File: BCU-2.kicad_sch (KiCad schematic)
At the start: 10 parts, among them J2 Conn_01x12_Male, J6 Conn_01x04_Male, J7 Conn_01x04_Male, U1 Teensy3.2

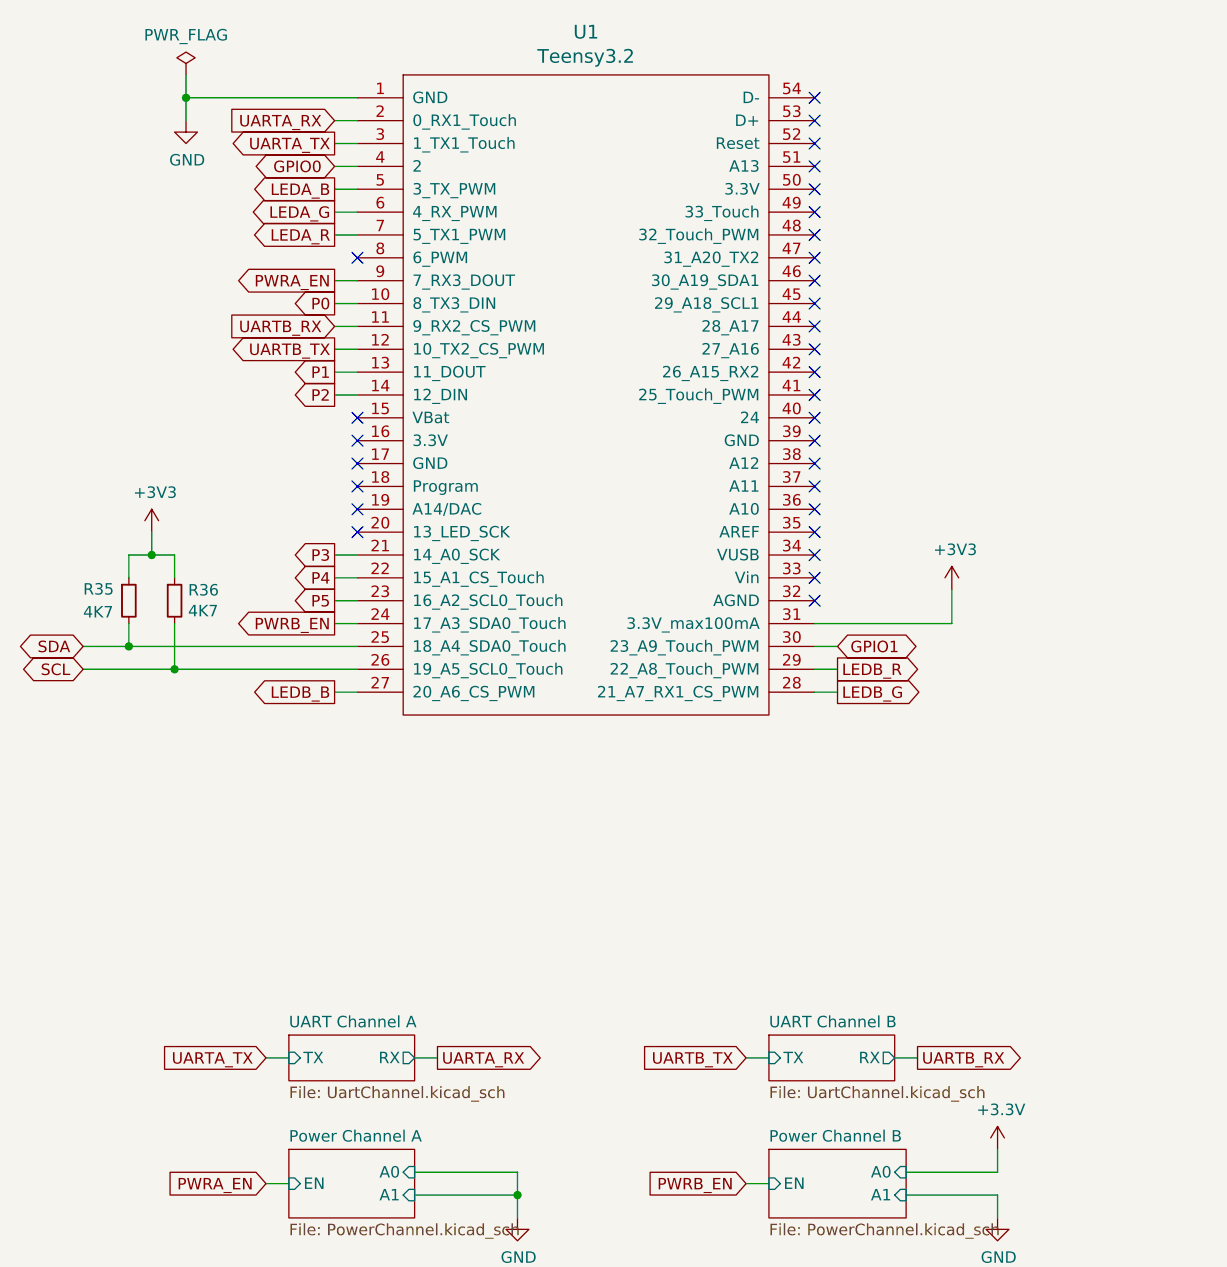
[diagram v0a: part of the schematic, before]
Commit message: Schematic: Remove UART channels
Signed-off-by: Geert Uytterhoeven <geert@linux-m68k.org>
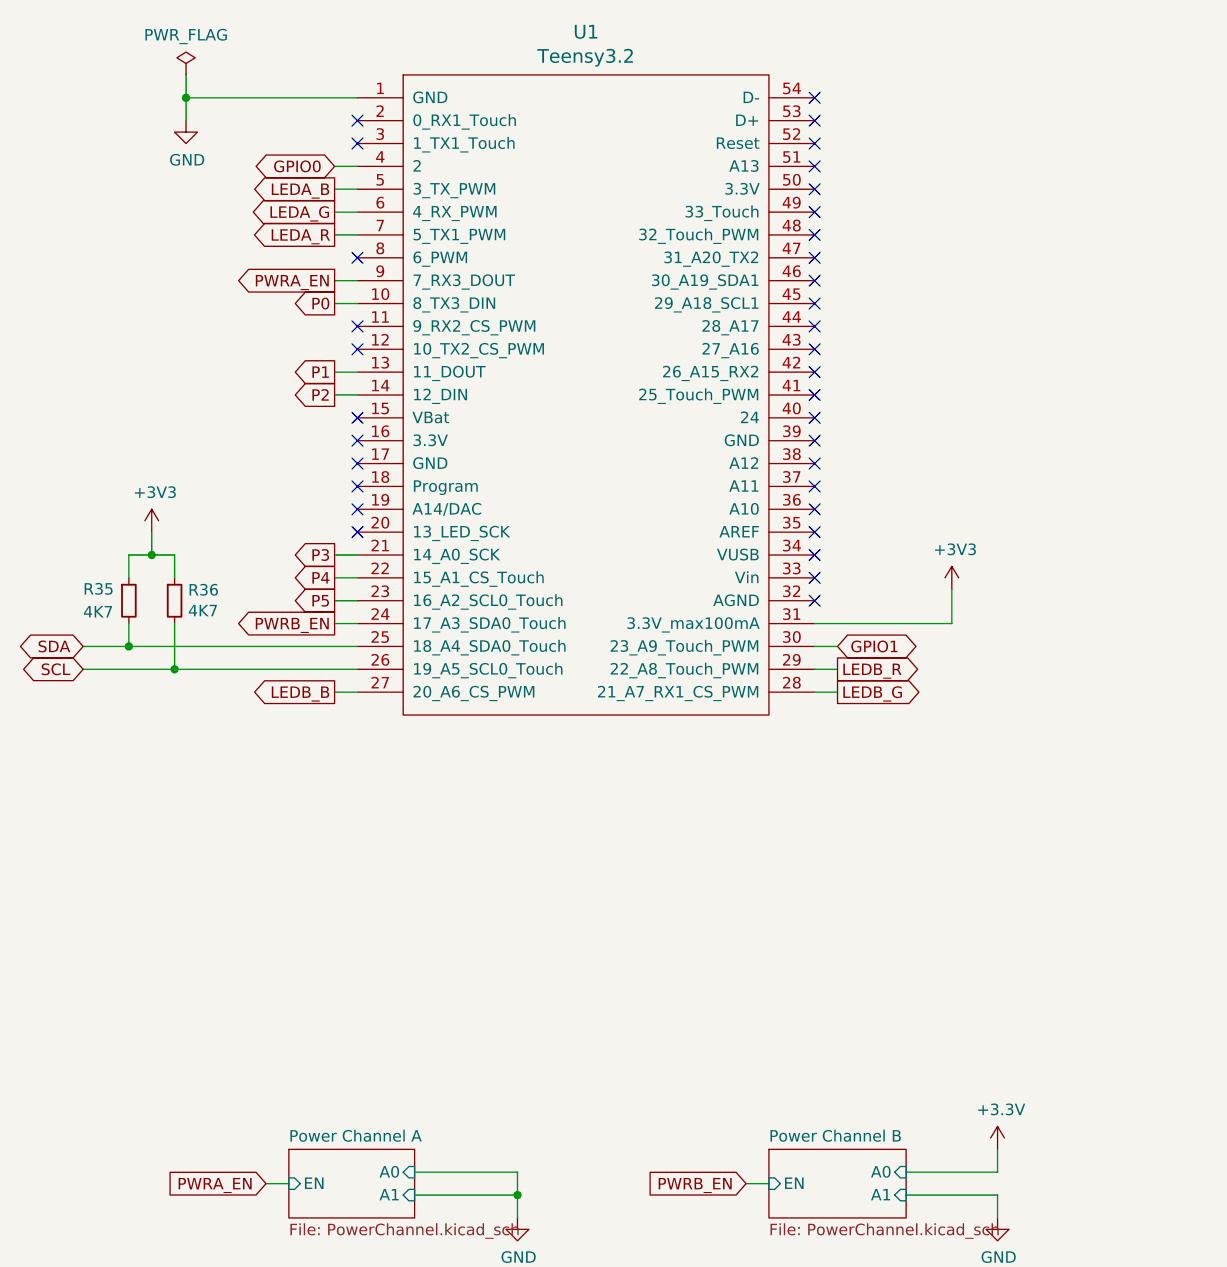
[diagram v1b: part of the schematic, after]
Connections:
- net UARTA_RX: no longer names the net of U1.2 (0_RX1_Touch)
- net UARTA_TX: no longer names the net of U1.3 (1_TX1_Touch)
- net UARTB_RX: no longer names the net of U1.11 (9_RX2_CS_PWM)
- net UARTB_TX: no longer names the net of U1.12 (10_TX2_CS_PWM)
- no-connect marks 30 -> 34
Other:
- removed sheet UART Channel A
- removed sheet UART Channel B

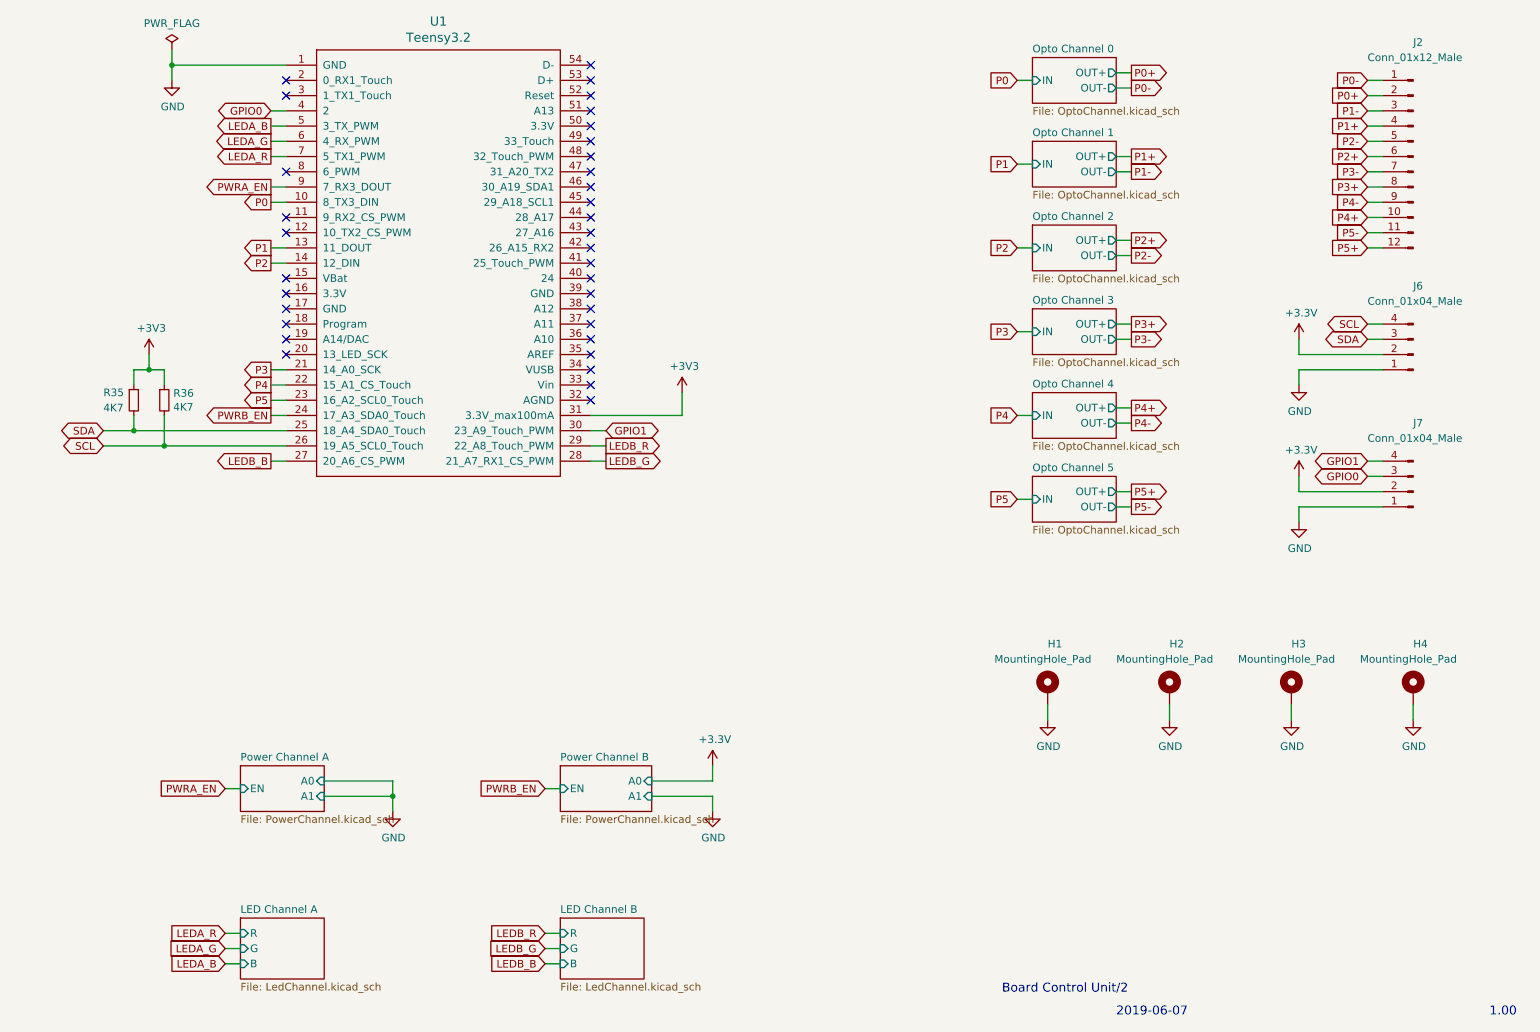
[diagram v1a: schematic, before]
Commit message: Schematic: Remove LED channels
Signed-off-by: Geert Uytterhoeven <geert@linux-m68k.org>
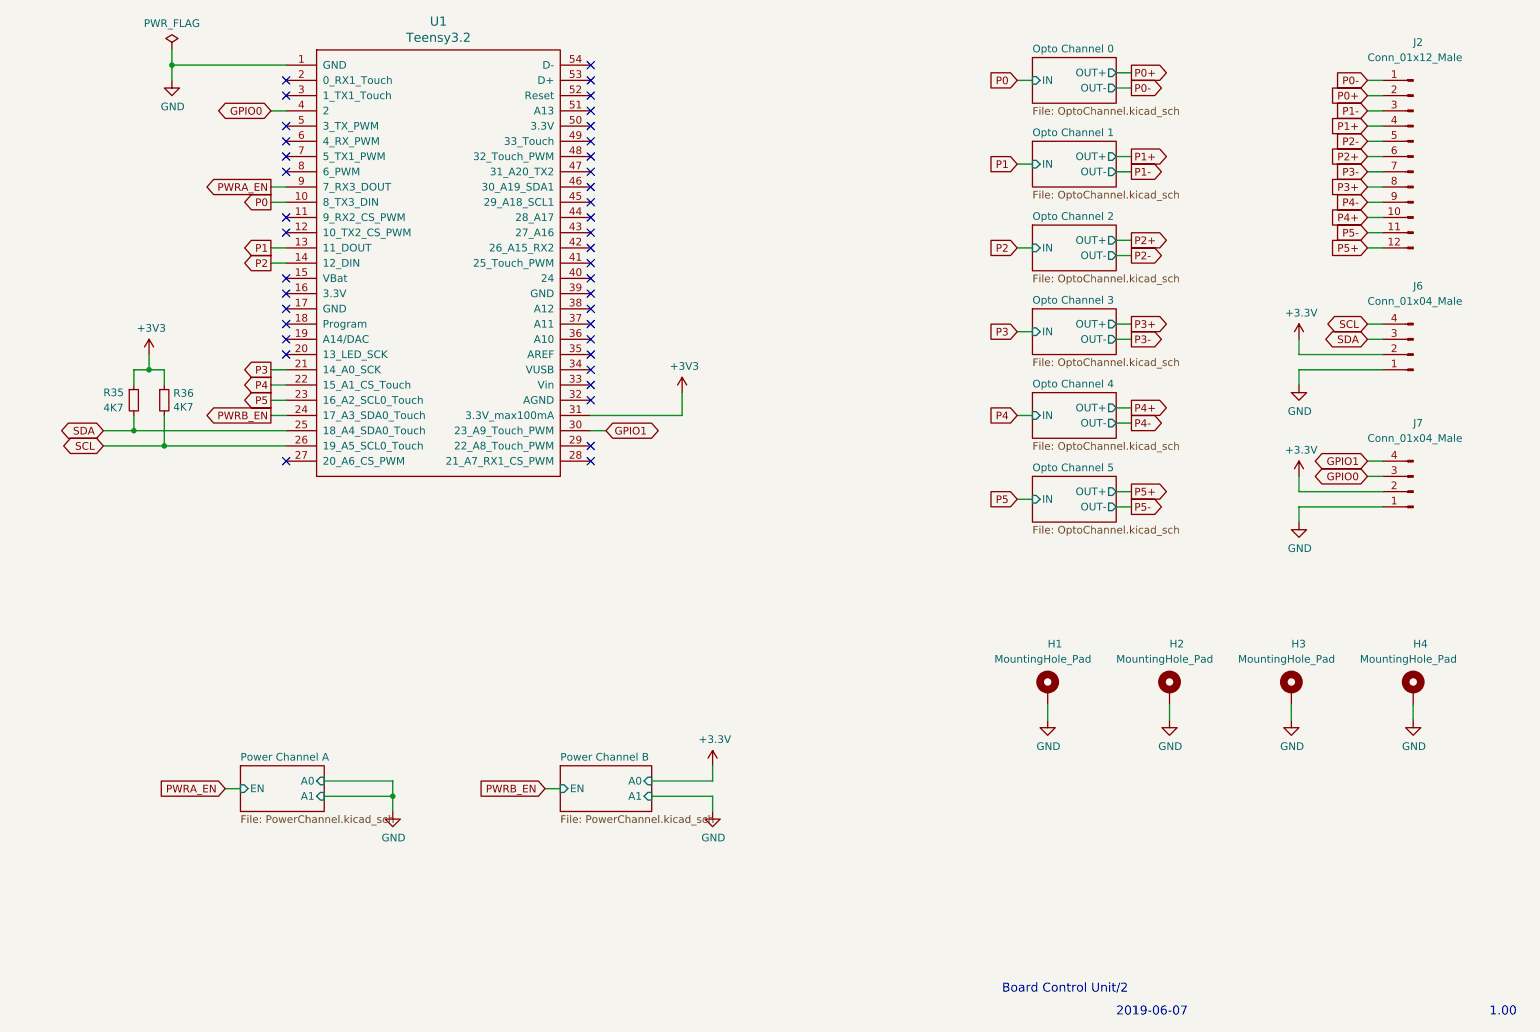
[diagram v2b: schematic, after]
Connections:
- net LEDA_B: no longer names the net of U1.5 (3_TX_PWM)
- net LEDA_G: no longer names the net of U1.6 (4_RX_PWM)
- net LEDA_R: no longer names the net of U1.7 (5_TX1_PWM)
- net LEDB_B: no longer names the net of U1.27 (20_A6_CS_PWM)
- net LEDB_G: no longer names the net of U1.28 (21_A7_RX1_CS_PWM)
- net LEDB_R: no longer names the net of U1.29 (22_A8_Touch_PWM)
- no-connect marks 34 -> 40
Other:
- removed sheet LED Channel A
- removed sheet LED Channel B

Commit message: Schematic: Remove GPIO expansion connector
Signed-off-by: Geert Uytterhoeven <geert@linux-m68k.org>
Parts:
- removed J7: Conn_01x04_Male, Connector_JST:JST_PH_B4B-PH-K_1x04_P2.00mm_Vertical, symbol Connector:Conn_01x04_Male
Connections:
- net GPIO0: no longer names the net of U1.4 (2)
- net GPIO1: no longer names the net of U1.30 (23_A9_Touch_PWM)
- no-connect marks 40 -> 42
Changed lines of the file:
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@@
   (no_connect (at 68.58 71.12))
   (no_connect (at 119.38 40.64))
+  (no_connect (at 119.38 96.52))
   (no_connect (at 68.58 45.72))
   (no_connect (at 119.38 38.1))
   (no_connect (at 68.58 81.28))
   (no_connect (at 68.58 60.96))
+  (no_connect (at 68.58 43.18))
   (no_connect (at 68.58 53.34))
   (no_connect (at 68.58 76.2))
@@
     (stroke (width 0) (type default) (color 0 0 0 0))
   )
-  (wire (pts (xy 248.92 101.6) (xy 251.46 101.6))
-    (stroke (width 0) (type default) (color 0 0 0 0))
-  )
   (wire (pts (xy 251.46 40.64) (xy 248.92 40.64))
     (stroke (width 0) (type default) (color 0 0 0 0))
   )
-  (wire (pts (xy 251.46 104.14) (xy 248.92 104.14))
-    (stroke (width 0) (type default) (color 0 0 0 0))
-  )
-  (wire (pts (xy 237.49 106.68) (xy 237.49 104.14))
-    (stroke (width 0) (type default) (color 0 0 0 0))
-  )
-  (wire (pts (xy 119.38 96.52) (xy 121.92 96.52))
-    (stroke (width 0) (type default) (color 0 0 0 0))
-  )
   (wire (pts (xy 207.01 92.71) (xy 209.55 92.71))
     (stroke (width 0) (type default) (color 0 0 0 0))
@@
     (stroke (width 0) (type default) (color 0 0 0 0))
   )
-  (wire (pts (xy 251.46 109.22) (xy 237.49 109.22))
-    (stroke (width 0) (type default) (color 0 0 0 0))
-  )
   (wire (pts (xy 251.46 83.82) (xy 237.49 83.82))
     (stroke (width 0) (type default) (color 0 0 0 0))
@@
     (stroke (width 0) (type default) (color 0 0 0 0))
   )
-  (wire (pts (xy 66.04 43.18) (xy 68.58 43.18))
-    (stroke (width 0) (type default) (color 0 0 0 0))
-  )
   (wire (pts (xy 129.54 154.94) (xy 139.7 154.94))
     (stroke (width 0) (type default) (color 0 0 0 0))
@@
     (stroke (width 0) (type default) (color 0 0 0 0))
   )
-  (wire (pts (xy 251.46 106.68) (xy 237.49 106.68))
-    (stroke (width 0) (type default) (color 0 0 0 0))
-  )
   (wire (pts (xy 248.92 78.74) (xy 251.46 78.74))
-    (stroke (width 0) (type default) (color 0 0 0 0))
-  )
-  (wire (pts (xy 237.49 109.22) (xy 237.49 111.76))
     (stroke (width 0) (type default) (color 0 0 0 0))
   )
@@
     )
   )
-  (global_label "GPIO0" (shape bidirectional) (at 66.04 43.18 180) (fields_autoplaced)
-    (effects (font (size 1.27 1.27)) (justify right))
-    (property "Intersheet References" "${INTERSHEET_REFS}" (id 0) (at 0 0 0)
-      (effects (font (size 1.27 1.27)) hide)
-    )
-  )
   (global_label "PWRA_EN" (shape input) (at 58.42 156.21 180) (fields_autoplaced)
     (effects (font (size 1.27 1.27)) (justify right))
@@
   (global_label "P1" (shape input) (at 190.5 52.07 180) (fields_autoplaced)
     (effects (font (size 1.27 1.27)) (justify right))
-    (property "Intersheet References" "${INTERSHEET_REFS}" (id 0) (at 0 0 0)
-      (effects (font (size 1.27 1.27)) hide)
-    )
-  )
-  (global_label "GPIO1" (shape bidirectional) (at 121.92 96.52 0) (fields_autoplaced)
-    (effects (font (size 1.27 1.27)) (justify left))
     (property "Intersheet References" "${INTERSHEET_REFS}" (id 0) (at 0 0 0)
       (effects (font (size 1.27 1.27)) hide)
@@
     )
   )
-  (global_label "GPIO1" (shape bidirectional) (at 248.92 101.6 180) (fields_autoplaced)
-    (effects (font (size 1.27 1.27)) (justify right))
-    (property "Intersheet References" "${INTERSHEET_REFS}" (id 0) (at 0 0 0)
-      (effects (font (size 1.27 1.27)) hide)
-    )
-  )
   (global_label "P4+" (shape output) (at 209.55 92.71 0) (fields_autoplaced)
     (effects (font (size 1.27 1.27)) (justify left))
@@
   )
   (global_label "PWRB_EN" (shape input) (at 111.76 156.21 180) (fields_autoplaced)
-    (effects (font (size 1.27 1.27)) (justify right))
-    (property "Intersheet References" "${INTERSHEET_REFS}" (id 0) (at 0 0 0)
-      (effects (font (size 1.27 1.27)) hide)
-    )
-  )
-  (global_label "GPIO0" (shape bidirectional) (at 248.92 104.14 180) (fields_autoplaced)
     (effects (font (size 1.27 1.27)) (justify right))
     (property "Intersheet References" "${INTERSHEET_REFS}" (id 0) (at 0 0 0)
@@
     (pin "1")
   )
-  (symbol (lib_id "Connector:Conn_01x04_Male") (at 256.54 106.68 180) (unit 1)
-    (in_bom yes) (on_board yes)
-    (property "Reference" "J7" (id 0) (at 256.54 95.25 0)
-      (effects (font (size 1.27 1.27)) (justify right))
-    )
-    (property "Value" "Conn_01x04_Male" (id 1) (at 248.92 97.79 0)
-      (effects (font (size 1.27 1.27)) (justify right))
-    )
-    (property "Footprint" "Connector_JST:JST_PH_B4B-PH-K_1x04_P2.00mm_Vertical" (id 2) (at 256.54 106.68 0)
-      (effects (font (size 1.27 1.27)) hide)
-    )
-    (property "Datasheet" "~" (id 3) (at 256.54 106.68 0)
-      (effects (font (size 1.27 1.27)) hide)
-    )
-    (pin "1")
-    (pin "2")
-    (pin "3")
-    (pin "4")
-  )
-  (symbol (lib_id "power:GND") (at 237.49 111.76 0) (unit 1)
-    (in_bom yes) (on_board yes)
-    (property "Reference" "#PWR0115" (id 0) (at 237.49 118.11 0)
-      (effects (font (size 1.27 1.27)) hide)
-    )
-    (property "Value" "GND" (id 1) (at 237.617 116.1542 0))
-    (property "Footprint" "" (id 2) (at 237.49 111.76 0)
-      (effects (font (size 1.27 1.27)) hide)
-    )
-    (property "Datasheet" "" (id 3) (at 237.49 111.76 0)
-      (effects (font (size 1.27 1.27)) hide)
-    )
-    (pin "1")
-  )
-  (symbol (lib_id "power:+3.3V") (at 237.49 104.14 0) (unit 1)
-    (in_bom yes) (on_board yes)
-    (property "Reference" "#PWR0116" (id 0) (at 237.49 107.95 0)
-      (effects (font (size 1.27 1.27)) hide)
-    )
-    (property "Value" "+3.3V" (id 1) (at 237.871 99.7458 0))
-    (property "Footprint" "" (id 2) (at 237.49 104.14 0)
-      (effects (font (size 1.27 1.27)) hide)
-    )
-    (property "Datasheet" "" (id 3) (at 237.49 104.14 0)
-      (effects (font (size 1.27 1.27)) hide)
-    )
-    (pin "1")
-  )
   (symbol (lib_id "Connector:Conn_01x12_Male") (at 256.54 50.8 0) (mirror y) (unit 1)
     (in_bom yes) (on_board yes)
@@
       (reference "#PWR0112") (unit 1) (value "+3V3") (footprint "")
     )
-    (path "/00000000-0000-0000-0000-00005ce94ab6"
-      (reference "#PWR0115") (unit 1) (value "GND") (footprint "")
-    )
-    (path "/00000000-0000-0000-0000-00005ce94abc"
-      (reference "#PWR0116") (unit 1) (value "+3.3V") (footprint "")
-    )
     (path "/00000000-0000-0000-0000-00005be8d10d/00000000-0000-0000-0000-00005ce3761d"
       (reference "C5") (unit 1) (value "100n") (footprint "Capacitor_SMD:C_0603_1608Metric_Pad1.05x0.95mm_HandSolder")
@@
       (reference "J6") (unit 1) (value "Conn_01x04_Male") (footprint "Connector_JST:JST_PH_B4B-PH-K_1x04_P2.00mm_Vertical")
     )
-    (path "/00000000-0000-0000-0000-00005ce94aad"
-      (reference "J7") (unit 1) (value "Conn_01x04_Male") (footprint "Connector_JST:JST_PH_B4B-PH-K_1x04_P2.00mm_Vertical")
-    )
     (path "/00000000-0000-0000-0000-00005be8d10d/00000000-0000-0000-0000-00005bf70897"
